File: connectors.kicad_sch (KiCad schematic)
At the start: 6 parts, among them J1 USB_C_Receptacle_USB2.0, J2 USB_C_Receptacle_USB2.0, J3 Screw_Terminal_01x02, J4 USB_A, U3 SRV05-4, U4 SRV05-4

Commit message: Wire more stuff
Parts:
- removed J1, J2: USB_C_Receptacle_USB2.0, Connector_USB:USB_C_Receptacle_G-Switch_GT-USB-7010ASV, symbol Connector:USB_C_Receptacle_USB2.0
- removed U3: SRV05-4, Package_TO_SOT_SMD:SOT-23-6, symbol Power_Protection:SRV05-4
- added F1: Fuse, symbol Device:Fuse
- added J1: U262-241N-4BV60, Connector_USB:USB_C_Receptacle_Amphenol_12401548E4-2A, symbol Connector:USB_C_Receptacle
- added J2: Conn_ARM_SWD_TagConnect_TC2030-NL, Connector:Tag-Connect_TC2030-IDC-NL_2x03_P1.27mm_Vertical, symbol Connector:Conn_ARM_SWD_TagConnect_TC2030-NL
- added U5: SRV05-4, Package_TO_SOT_SMD:SOT-23-6, symbol Power_Protection:SRV05-4
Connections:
- net CC_PORT0.CC1: now also J1.A5 (CC1)
- net CC_PORT0.CC2: now also J1.B5 (CC2)
- net D+: now also J1.A6 (D+), J1.B6 (D+); no longer U4.1 (IO1)
- net D-: now also J1.A7 (D-), J1.B7 (D-); no longer U4.3 (IO2)
- net GND: now also J1.A1 (GND), J1.A12 (GND), J1.B1 (GND), J1.B12 (GND), J1.S1 (SHIELD), J2.5 (GND), U5.2 (VN)
- net VBUS_PORT0: now also J1.A4 (VBUS), J1.A9 (VBUS), J1.B4 (VBUS), J1.B9 (VBUS); no longer U4.5 (VP)
- net Vdrive: now also F1.1; no longer J3.1 (Pin_1)
- new net: F1.2, J3.1 (Pin_1)
- new net +3V3: J2.1 (VCC), U5.5 (VP)
- new net SWD.SWDCLK: J2.4 (SWCLK), U5.6 (IO4)
- new net SWD.SWDIO: J2.2 (SWDIO), U5.1 (IO1)
- new net SWD.SWO: U5.3 (IO2)
- new net ~{RESET}: J2.3 (~{RESET}), U5.4 (IO3)
- no-connect marks 0 -> 14
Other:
- note added: "Vdrive must not exceed 15V, due to AMS1117"
- note removed: "- How to do ESD protection on D- and D+? - Do PORT0.D- and PORTA.D+ need to be separated electrically?"
- note removed: "Can PORT1 D-, D+, SBU1, SBU2 be left floating?"
- moved on the sheet: J3, J4, U4

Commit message: Whole bunch of changes to all kinds of things
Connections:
- net D+: now also J4.2 (D-); no longer J4.3 (D+)
- net D-: now also J4.3 (D+); no longer J4.2 (D-)
- net SWD.SWO: no longer names the net of U5.3 (IO2)
- no-connect marks 14 -> 15
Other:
- note added: "Use simpler USBC plug"
- moved on the sheet: F1, J1, J2, J3, J4, U4

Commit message: WIP on vconn
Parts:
- added D1: SLD15-018, https://nl.mouser.com/datasheet/2/240/media-3323920.pdf, symbol Device:D_TVS
- F1: value Fuse -> iMaXX-H7810; footprint (none) -> usb-zekers:iMaXX-H7810
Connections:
- net GND: now also D1.1 (A1)
- net Vdrive: now also D1.2 (A2)
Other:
- moved on the sheet: F1, J3

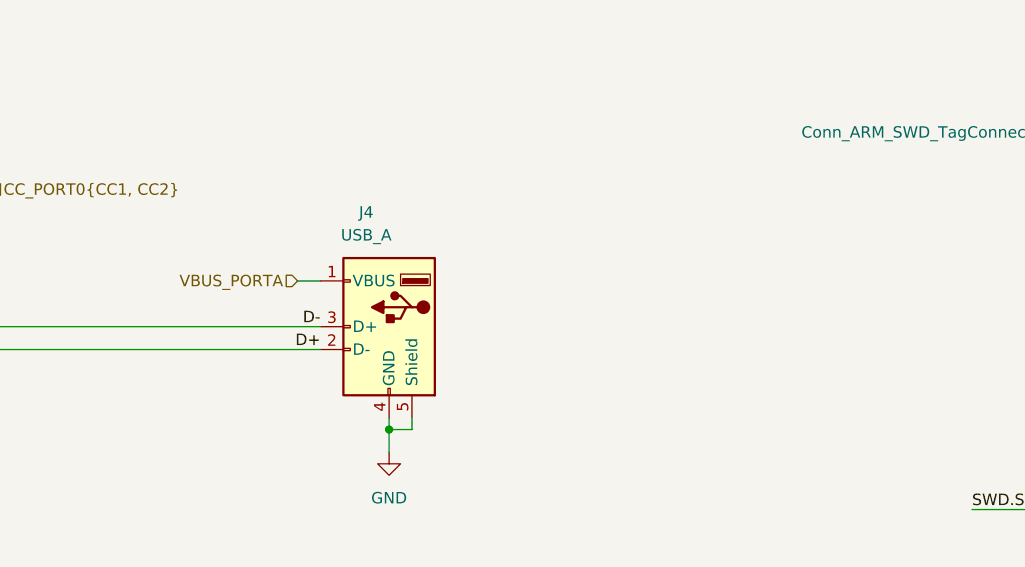
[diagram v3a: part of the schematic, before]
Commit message: Wire up vconn and analog pins
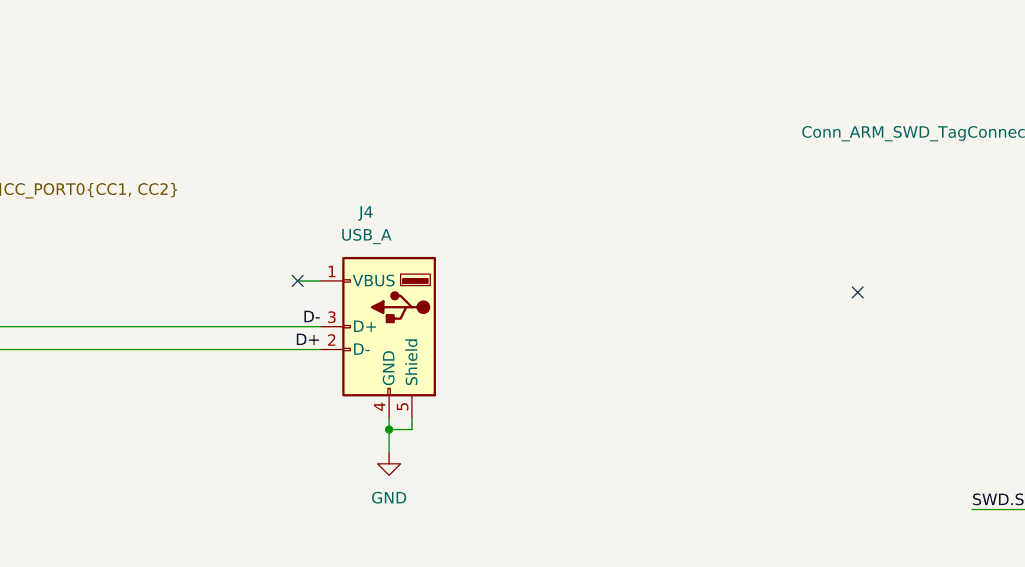
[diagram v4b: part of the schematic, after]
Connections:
- net VBUS_PORTA: no longer names the net of J4.1 (VBUS)
- no-connect marks 15 -> 17
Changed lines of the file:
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@@
+	)
+	(no_connect
+		(at 181.61 115.57)
 	)
 	(no_connect
@@
 	(no_connect
 		(at 62.23 137.16)
+	)
+	(no_connect
+		(at 119.38 114.3)
 	)
 	(no_connect
@@
 		)
 	)
-	(hierarchical_label "VBUS_PORTA"
-		(shape input)
-		(at 119.38 114.3 180)
-		(fields_autoplaced yes)
-		(effects
-			(font
-				(size 1.27 1.27)
-			)
-			(justify right)
-		)
-	)

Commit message: Wire up VCONN_FLGn
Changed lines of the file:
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@@
 	(text "Vdrive must not exceed 15V, due to AMS1117"
 		(exclude_from_sim no)
-		(at 121.666 21.336 0)
+		(at 173.228 19.304 0)
 		(effects
 			(font

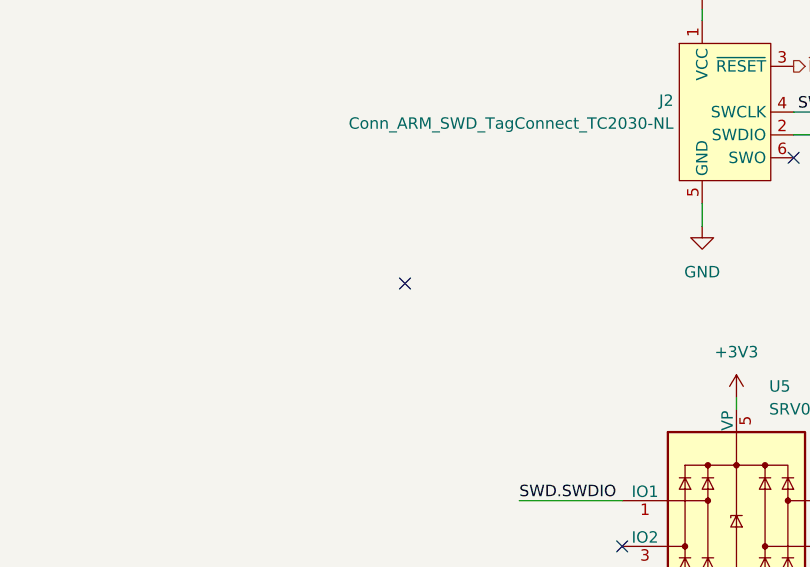
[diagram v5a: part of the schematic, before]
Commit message: Fix ERC errors, swap out mosfets for NVC chip
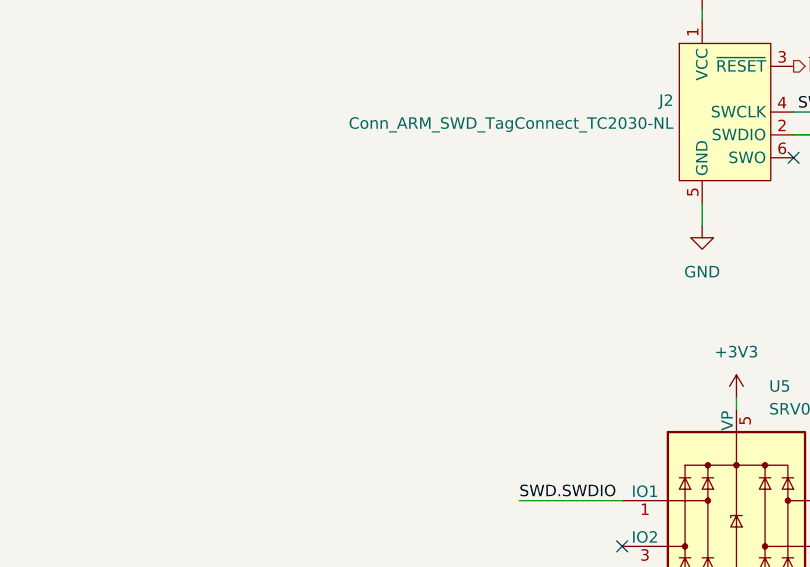
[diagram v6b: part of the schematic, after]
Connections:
- no-connect marks 17 -> 16
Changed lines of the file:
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@@
-	)
-	(no_connect
-		(at 181.61 115.57)
 	)
 	(no_connect

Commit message: more footprints
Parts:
- removed J1: U262-241N-4BV60, Connector_USB:USB_C_Receptacle_Amphenol_12401548E4-2A, symbol Connector:USB_C_Receptacle
- added FB1: FCM1608KF-601T05, Inductor_SMD:L_0603_1608Metric, symbol Device:FerriteBead
- added J5: USB4105-GF-A-120, Connector_USB:USB_C_Receptacle_GCT_USB4105-xx-A_16P_TopMnt_Horizontal, symbol Connector:USB_C_Receptacle_USB2.0_14P
- D1: footprint https://nl.mouser.com/datasheet/2/240/media-3323920.pdf -> (none)
- J3: footprint (none) -> TerminalBlock_Phoenix:TerminalBlock_Phoenix_PTSM-0,5-2-2,5-V-SMD_1x02-1MP_P2.50mm_Vertical
- J4: value USB_A -> 48037-2200; footprint (none) -> Connector_USB:USB_A_Molex_48037-2200_Horizontal
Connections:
- net CC_PORT0.CC1: now also J5.A5 (CC1)
- net CC_PORT0.CC2: now also J5.B5 (CC2)
- net D+: now also J5.A6 (D+), J5.B6 (D+)
- net D-: now also J5.A7 (D-), J5.B7 (D-)
- net GND: now also J5.A1 (GND), J5.A12 (GND), J5.B1 (GND), J5.B12 (GND), J5.S1 (SHIELD)
- net VBUS_PORT0: now also J5.A4 (VBUS), J5.A9 (VBUS), J5.B4 (VBUS), J5.B9 (VBUS)
- net Vdrive: now also FB1.2; no longer F1.1
- new net: F1.1, FB1.1
- no-connect marks 16 -> 6
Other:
- note removed: "Use simpler USBC plug"
- moved on the sheet: D1, F1, J3, J4
